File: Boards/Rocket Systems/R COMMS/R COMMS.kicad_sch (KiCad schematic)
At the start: 71 parts, among them IC1 BC846BLT1G, IC2 NSVT30010MXV6T1G, IC3 THVD2412VDR, J2 22285061, J4 MEM2061-01-188-00-A_REVA, J5 5023520600, J6 SMARA_CONNECTOR, U3 SX1280IMLTRT, U4 NRF21540-QDAA-R, U6 IP4220CZ6, U7 IP4220CZ6, U8 STLM20DD9F, U9 VLMKG3400-GS08

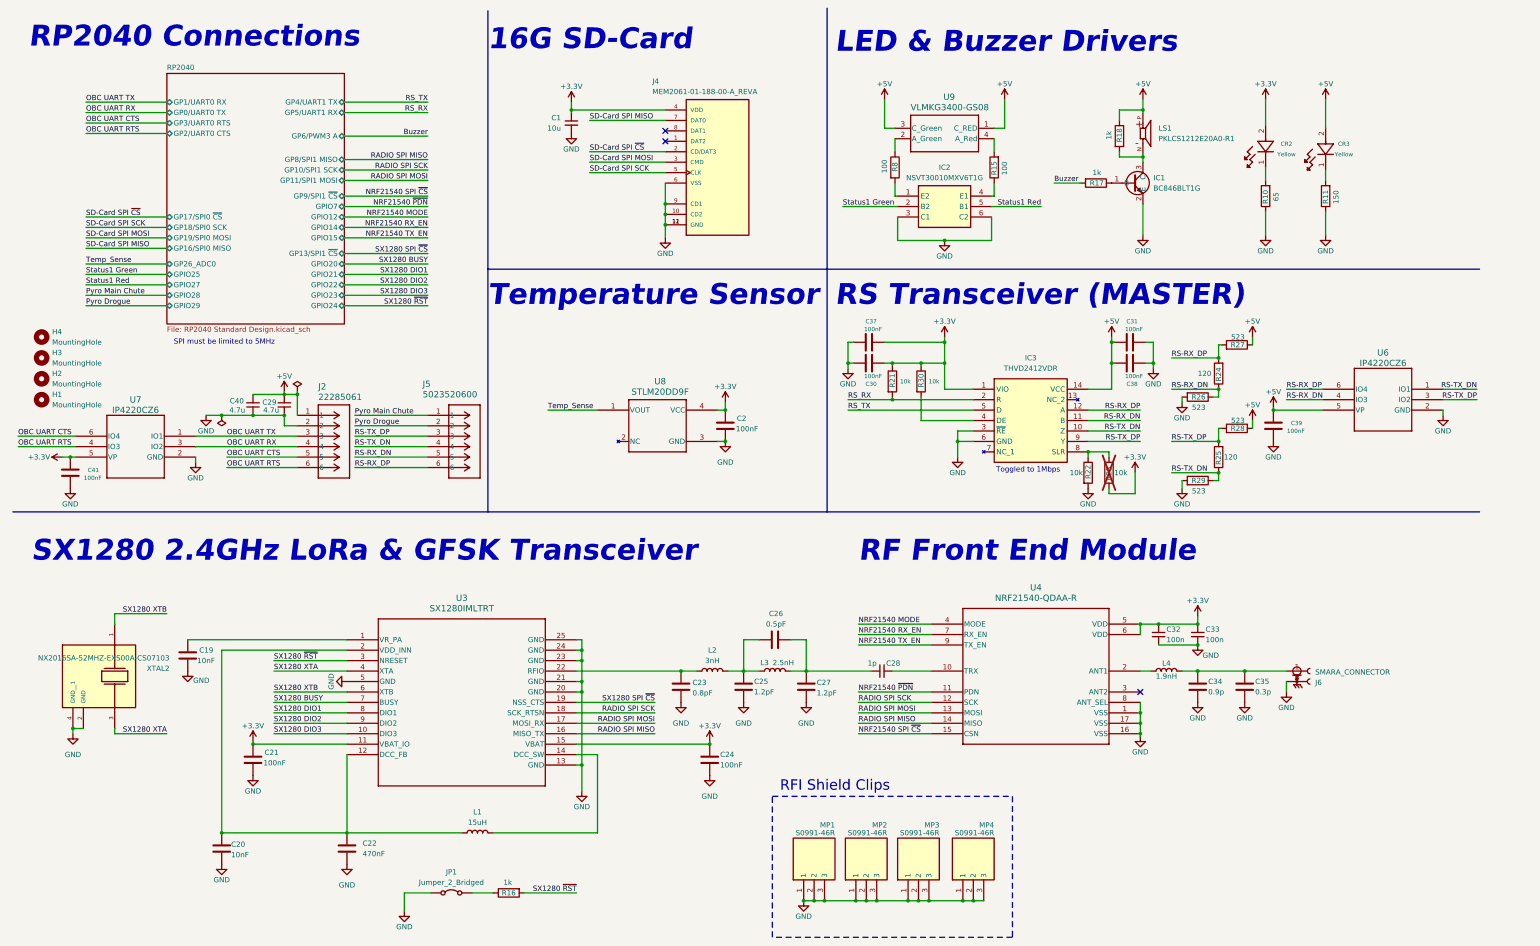
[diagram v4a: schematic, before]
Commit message: TVCS refactor
Muitas alterações e correções na placa TVCSO:
Novo ADC, filtros passa baixo, novo RS transceiver, reformulação de
conexões
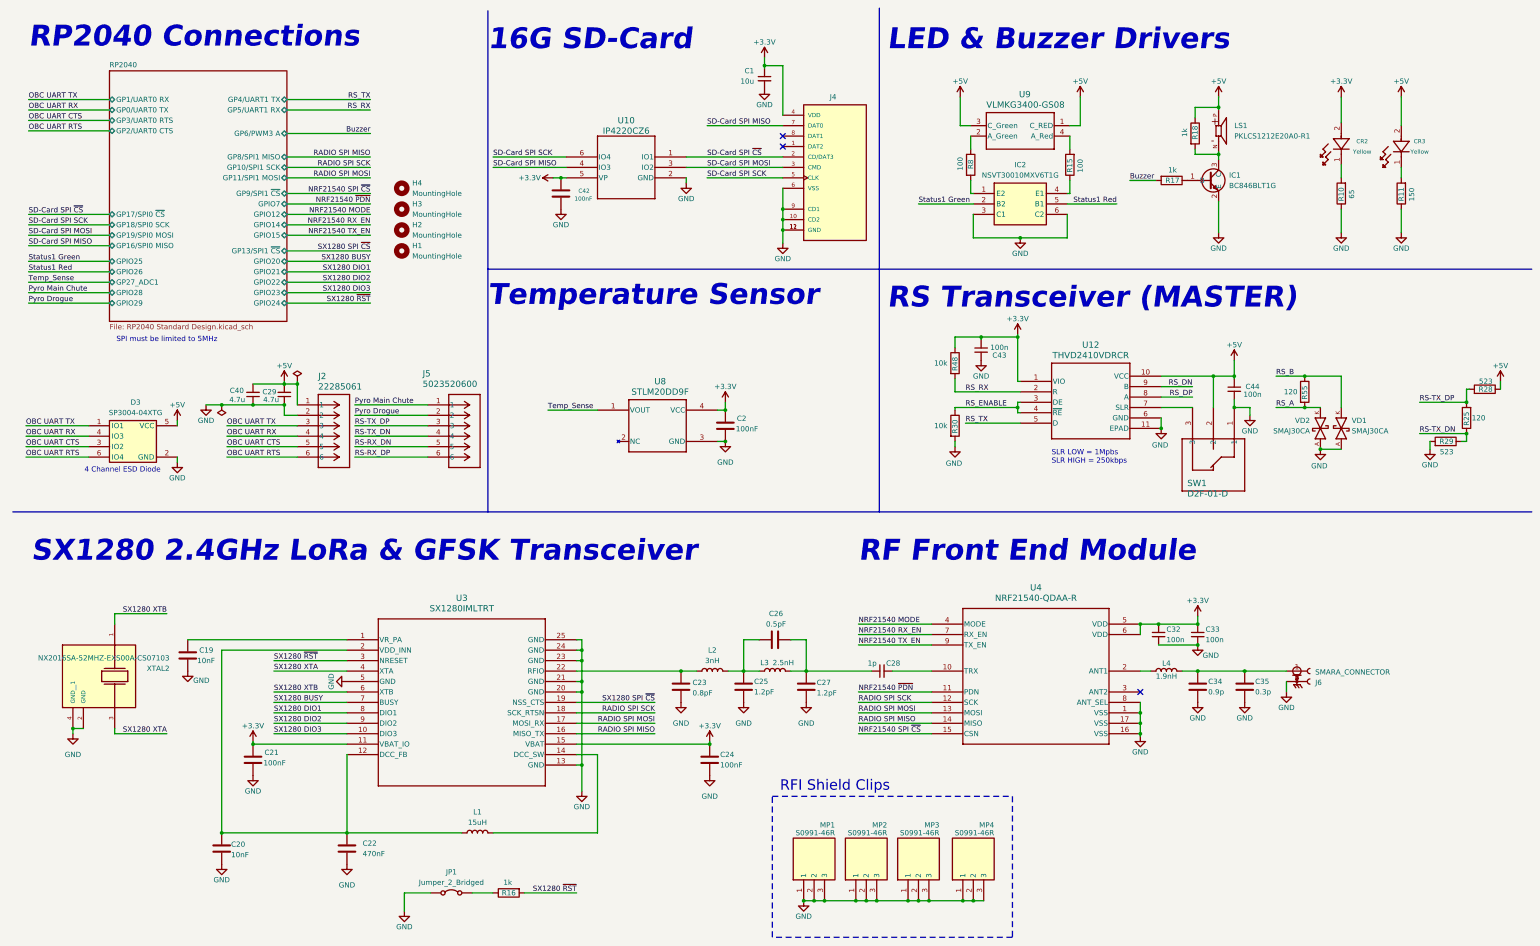
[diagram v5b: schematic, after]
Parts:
- removed C30, C31, C37, C38, C39, C41: 100nF, Capacitor-0402:Capacitor_0402, symbol Device:C
- removed IC3: THVD2412VDR, THVD2412VDR:SOIC127P600X175-14N, symbol THVD2412VDR:THVD2412VDR
- removed R21, R22, R23: 10k, Resistor-0402:RES_0402, symbol Device:R
- removed R24: 120, Resistor-0402:RES_0402, symbol Device:R
- removed R26, R27: 523, Resistor-0402:RES_0402, symbol Device:R
- removed U6, U7: IP4220CZ6, IP4220CZ6:SOT457_NEX, symbol IP4220CZ6F:IP4220CZ6
- added C42: 100nF, Capacitor-0402:Capacitor_0402, symbol Device:C
- added C43, C44: 100n, Capacitor-0402:Capacitor_0402, symbol Device:C_Small
- added D3: SP3004-04XTG, TVS-SP3004:SOT563_LTF, symbol SP3004-04XTG:SP3004-04XTG
- added R48: 10k, Resistor-0402:RES_0402, symbol Device:R
- added R55: 120, Resistor-0603:RES_0603, symbol Device:R
- added SW1: D2F-01-D, D2F-01-D_OMR, symbol Switch_D2F-01:D2F-01-D
- added U10: IP4220CZ6, IP4220CZ6:SOT457_NEX, symbol IP4220CZ6F:IP4220CZ6
- added U12: THVD2410VDRCR, VSON10_DRC_TEX, symbol THVD2410VDRCR:THVD2410VDRCR
- added VD1, VD2: SMAJ30CA, symbol SMAJ30CA:SMAJ30CA
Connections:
- net +3.3V: now also C42.1, C43.2, R48.1, U10.5 (VP), U12.1 (VIO); no longer R30.1
- net +5V: now also C44.1, D3.5 (VCC), SW1.2, U12.10 (VCC)
- net GND: now also R30.2, C42.2, C43.1, C44.2, D3.2 (GND), SW1.1, U10.2 (GND), U12.11 (EPAD), U12.6 (GND), VD1.A, VD2.A
- net OBC UART CTS: now also D3.3 (IO2)
- net OBC UART RTS: now also D3.6 (IO4)
- net OBC UART RX: now also D3.4 (IO3)
- net OBC UART TX: now also D3.1 (IO1)
- net RS_RX: now also R48.2, U12.2 (R)
- net RS_TX: now also U12.5 (D)
- net SD-Card SPI MISO: now also U10.4 (IO3)
- net SD-Card SPI MOSI: now also U10.3 (IO2)
- net SD-Card SPI SCK: now also U10.6 (IO4)
- net SD-Card SPI ~{CS}: now also U10.1 (IO1)
- new net: SW1.3, U12.7 (SLR)
- new net RS_A: R55.2, VD2.K
- new net RS_B: R55.1, VD1.K
- new net RS_DN: U12.9 (B)
- new net RS_DP: U12.8 (A)
- new net RS_ENABLE: R30.1, U12.3 (DE), U12.4 (~{RE})
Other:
- sheet RP2040 ports: added GP27_ADC1, GPIO26; removed GP26_ADC0, GPIO27
- note added: "4 Channel ESD Diode"
- note added: "SLR LOW = 1Mpbs SLR HIGH = 250kbps"
- note removed: "Toggled to 1Mbps"
- title: Rocket Communication System -> On Board Computer
- moved on the sheet: C1, C29, C40, CR2, CR3, H1, H2, H3, H4, IC1, IC2, J2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

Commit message: small pinout update
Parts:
- removed R25: 120, Resistor-0402:RES_0402, symbol Device:R
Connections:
- net RS_A is gone; now on net RS_DP: R55.2, VD2.K
- net RS_B is gone; now on net RS_DN: R55.1, VD1.K
- net Pyro Drogue: no longer J5.2
- net Pyro Main Chute: no longer J5.1
- net RS_DN: now also J5.1, R28.2
- net RS_DP: now also J5.2, R29.1
- net RS-RX_DN: no longer names the net of J5.5
- net RS-RX_DP: no longer names the net of J5.6
- net RS-TX_DN: no longer names the net of J5.4
- net RS-TX_DN: no longer R29.1
- net RS-TX_DP: no longer names the net of J5.3
- net RS-TX_DP: no longer R28.2
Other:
- note added: "Mudar connector para um de 2"
- moved on the sheet: R28, R29, R55, VD1, VD2

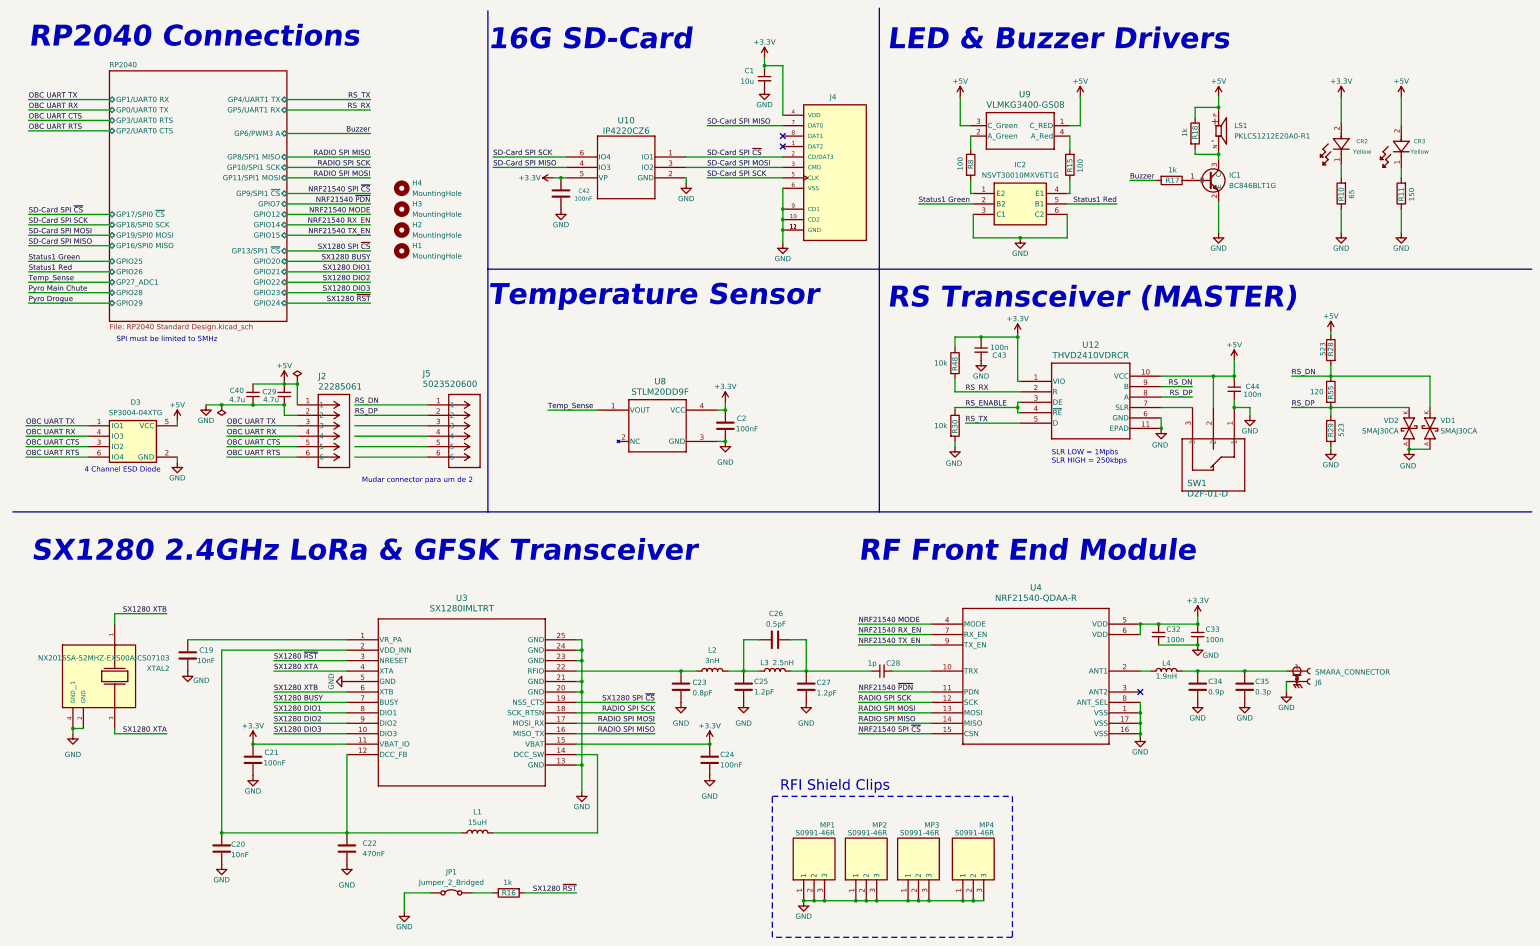
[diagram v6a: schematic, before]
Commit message: OBC a Navigator Updates
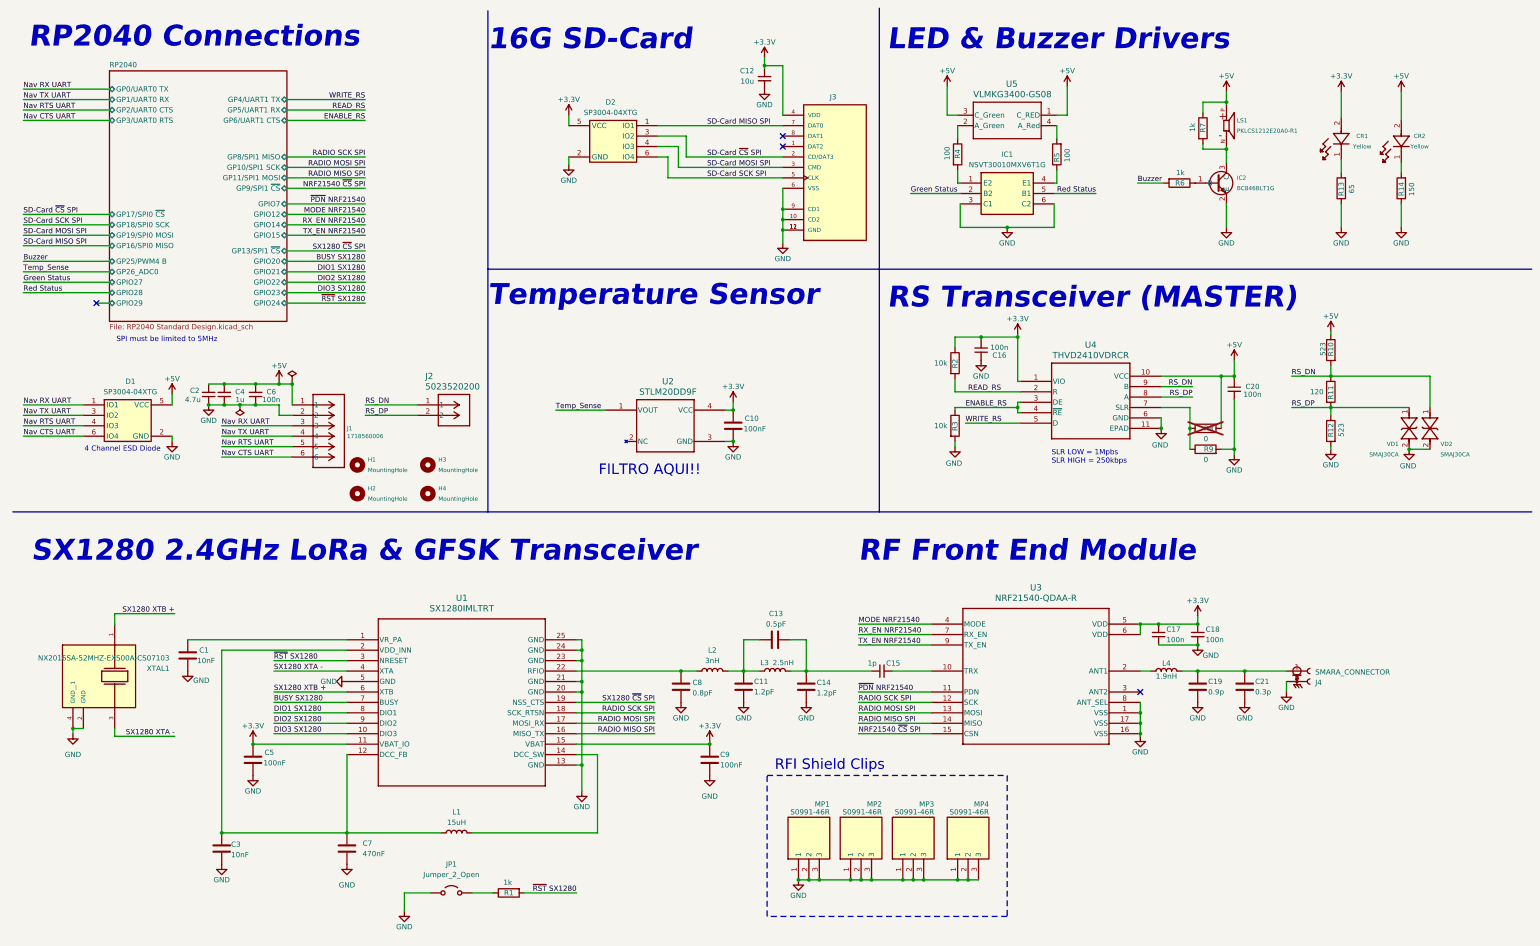
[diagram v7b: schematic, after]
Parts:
- removed C29: 4.7u, Capacitor-0402:Capacitor_0402, symbol Device:C_Small
- removed C42: 100nF, Capacitor-0402:Capacitor_0402, symbol Device:C
- removed J2: 22285061, CONN Male Header:CONN_SD-42375-001_M320_06_MOL, symbol PinCon_22285061:22285061
- removed J5: 5023520600, 5023520600:CONN06_502352_MOL, symbol 5023520600:5023520600
- removed JP1: Jumper_2_Bridged, Jumper:SolderJumper-2_P1.3mm_Open_RoundedPad1.0x1.5mm, symbol Jumper:Jumper_2_Bridged
- removed SW1: D2F-01-D, D2F-01-D_OMR, symbol Switch_D2F-01:D2F-01-D
- removed U10: IP4220CZ6, IP4220CZ6:SOT457_NEX, symbol IP4220CZ6F:IP4220CZ6
- added C4: 1u, Capacitor-0402:Capacitor_0402, symbol Device:C_Small
- added C6: 100n, Capacitor-0402:Capacitor_0402, symbol Device:C_Small
- added D2: SP3004-04XTG, TVS-SP3004:SOT563_LTF, symbol SP3004-04XTG:SP3004-04XTG
- added J1: 1718560006, 6 Male Conn:CONN06_1718560006_MOL, symbol 1718560006:1718560006
- added J2: 5023520200, Molex 2 Conn:CONN02_502352_MOL, symbol DuraClick_2Conn:5023520200
- added JP1: Jumper_2_Open, Jumper:SolderJumper-2_P1.3mm_Open_RoundedPad1.0x1.5mm, symbol Jumper:Jumper_2_Open
- added R8, R9: 0, Resistor-0402:RES_0402, symbol Device:R
- U4: renamed from U12; footprint VSON10_DRC_TEX -> THVD2410VDRCR:VSON10_DRC_TEX
- VD1, VD2: footprint (none) -> SMAJ30CA:SMASeries_LTF
- renumbered C19 to C1, C2 to C10, C25 to C11, C1 to C12, C26 to C13, C27 to C14, C28 to C15, C43 to C16, C32 to C17, C33 to C18, C34 to C19, C40 to C2, C44 to C20, C35 to C21, C20 to C3, C21 to C5, C22 to C7, C23 to C8, C24 to C9, CR2 to CR1, CR3 to CR2, D3 to D1, IC2 to IC1, IC1 to IC2, J4 to J3, J6 to J4, R16 to R1, R28 to R10, R55 to R11, R29 to R12, R10 to R13, R11 to R14, R48 to R2, R30 to R3, R8 to R4, R15 to R5, R17 to R6, R18 to R7, U3 to U1, U8 to U2, U4 to U3, U9 to U5, XTAL2 to XTAL1
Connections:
- net +3.3V: now also D2.5 (VCC)
- net +5V: now also C4.2, C6.2, J1.1, R8.2
- net GND: now also VD1.2, VD2.2, C4.1, C6.1, D2.2 (GND), J1.2, JP1.1 (A), R9.2; no longer VD1.A, VD2.A
- net RS_DN: now also VD2.1, J2.1; no longer VD1.K
- net RS_DP: now also VD1.1, J2.2; no longer VD2.K
- net at U4.7 (SLR): now also R8.1, R9.1
- net at R1.1: now also JP1.2 (B)
- net NRF21540 MODE renamed MODE NRF21540
- net NRF21540 RX_EN renamed RX_EN NRF21540
- net NRF21540 SPI ~{CS} renamed NRF21540 ~{CS} SPI
- net NRF21540 TX_EN renamed TX_EN NRF21540
- net NRF21540 ~{PDN} renamed ~{PDN} NRF21540
- net OBC UART CTS renamed Nav TX UART
- net Nav TX UART: now also J1.4
- net OBC UART RTS renamed Nav CTS UART
- net Nav CTS UART: now also J1.6
- net OBC UART RX renamed Nav RTS UART
- net Nav RTS UART: now also J1.5
- net OBC UART TX renamed Nav RX UART
- net Nav RX UART: now also J1.3
- net RADIO SPI MISO renamed RADIO MISO SPI
- net RADIO SPI MOSI renamed RADIO MOSI SPI
- net RADIO SPI SCK renamed RADIO SCK SPI
- net RS_ENABLE renamed ENABLE_RS
- net RS_RX renamed READ_RS
- net RS_TX renamed WRITE_RS
- net SD-Card SPI MISO renamed SD-Card MISO SPI
- net SD-Card MISO SPI: now also D2.1 (IO1)
- net SD-Card SPI MOSI renamed SD-Card MOSI SPI
- net SD-Card MOSI SPI: now also D2.4 (IO3)
- net SD-Card SPI SCK renamed SD-Card SCK SPI
- net SD-Card SCK SPI: now also D2.6 (IO4)
- net SD-Card SPI ~{CS} renamed SD-Card  ~{CS} SPI
- net SD-Card  ~{CS} SPI: now also D2.3 (IO2)
- net SX1280 BUSY renamed BUSY SX1280
- net SX1280 DIO1 renamed DIO1 SX1280
- net SX1280 DIO2 renamed DIO2 SX1280
- net SX1280 DIO3 renamed DIO3 SX1280
- net SX1280 SPI ~{CS} renamed SX1280 ~{CS} SPI
- net SX1280 XTA renamed SX1280 XTA -
- net SX1280 XTB renamed SX1280 XTB +
- net SX1280 ~{RST} renamed ~{RST} SX1280
- net Status1 Green renamed Green Status
- net Status1 Red renamed Red Status
- no-connect marks 3 -> 4
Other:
- sheet RP2040 ports: added GP25/PWM4 B, GP26_ADC0, GP6/UART1 CTS, GPIO27; removed GP27_ADC1, GP6/PWM3 A, GPIO25, GPIO26
- note added: "FILTRO AQUI!!"
- note removed: "Mudar connector para um de 2"
- moved on the sheet: C10, C2, CR1, CR2, D1, IC1, IC2, L1, LS1, MP1, MP2, MP3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
